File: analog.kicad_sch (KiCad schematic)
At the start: 51 parts, among them J10 Sensor harness, U13 ADS1115

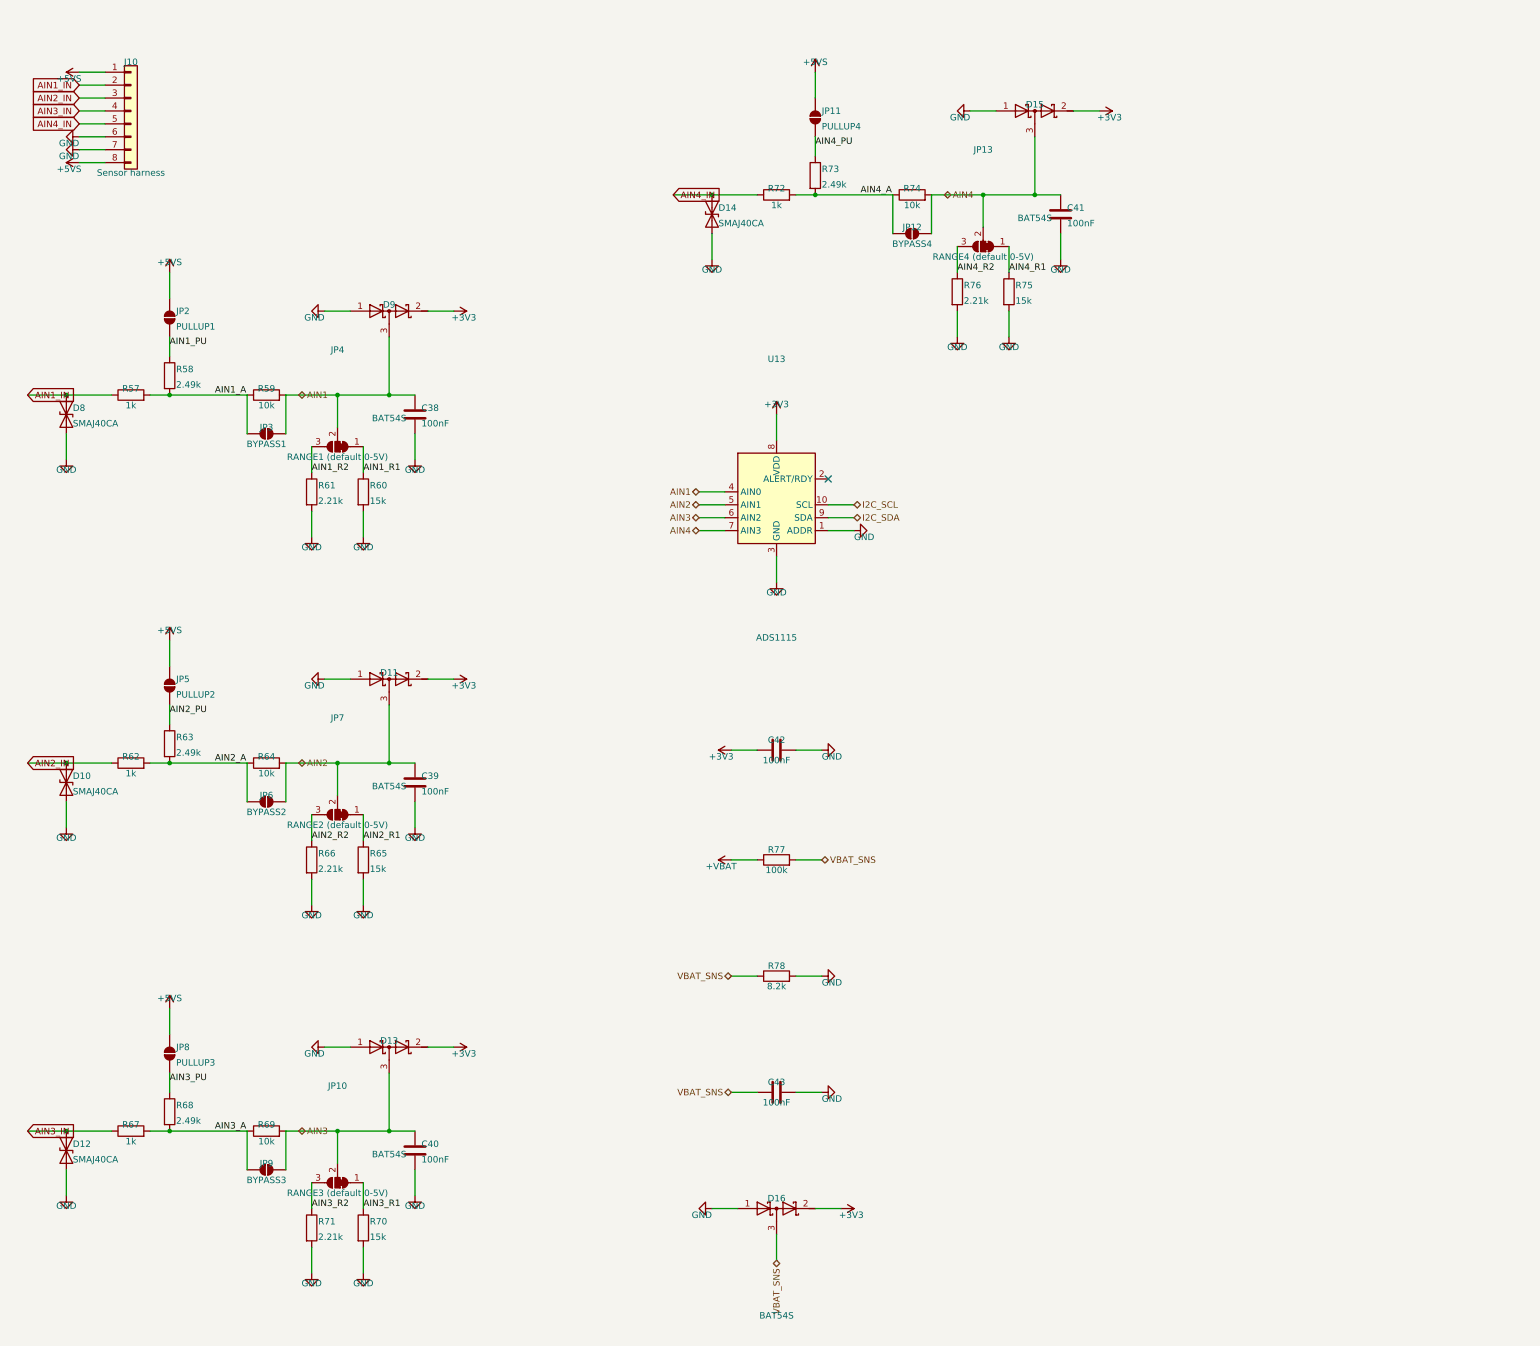
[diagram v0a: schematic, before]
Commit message: Re-scope the fork as a carrier board: no power section, differential analog, K-line
The shield idea does not survive measurement. Component courtyard on the
parent is 3052 mm2 over an 84 x 100 board -- 36% packing, not the 50% I had
been estimating -- and a DevKitC-1 is 63 x 25.5 = 1607 mm2. The parts alone
were 1.4x the whole dev board. So this is a carrier the dev board plugs into,
not a shield that fits on top of one.

Power section deleted entirely. It was 1746 mm2, 57% of the board, for two
rails the DevKitC-1 already makes from its USB-C. Gone: both LM5164 bucks and
everything around them, the LM74700 ideal diode, the reverse-battery FET, the
three electrolytic cans, the 12 V input, and the sensor-rail load switch.
Both rails are now inputs, taken up through the sockets -- which reverses the
earlier "feed 5 V only" rule, because there is no longer a second regulator
to parallel against.

Hold-up is a supercapacitor, not electrolytics. The first sizing was wrong:
energy goes as V-squared and the usable window at 5 V is 4.2 -> 3.6 V, so
2000 uF buys 12.5 ms, not the ~50 ms claimed. 0.5 F over the same window is
2.5 s, in less area than one of the 100 V cans it replaces. Low-ESR
cylindrical cells specifically -- coin EDLCs are 30-200 ohm and cannot source
120 mA at all.

Analog runs differentially. The board is grounded twice now, through the
sensor loom and through USB by way of a charger elsewhere in the car, and a
few hundred mV of chassis drop is 6% of a 0-5 V channel -- which makes the
0.1% dividers pointless. The correction has to be at the divider, not the
ADC, so the sensor ground comes back as a Kelvin wire through a matched
attenuator. Two ADS1115s, because one MUX only offers three channels against
a shared negative.

K-line added, discrete rather than an L9637D: that part's TXD threshold is
0.7*VCC = 3.5 V and a 3.3 V GPIO cannot meet it. Low-side 2N7002, clamped
22k/10k receiver, optional ISO 9141 tester pull-up on a jumper.

Pin map regrouped by boa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
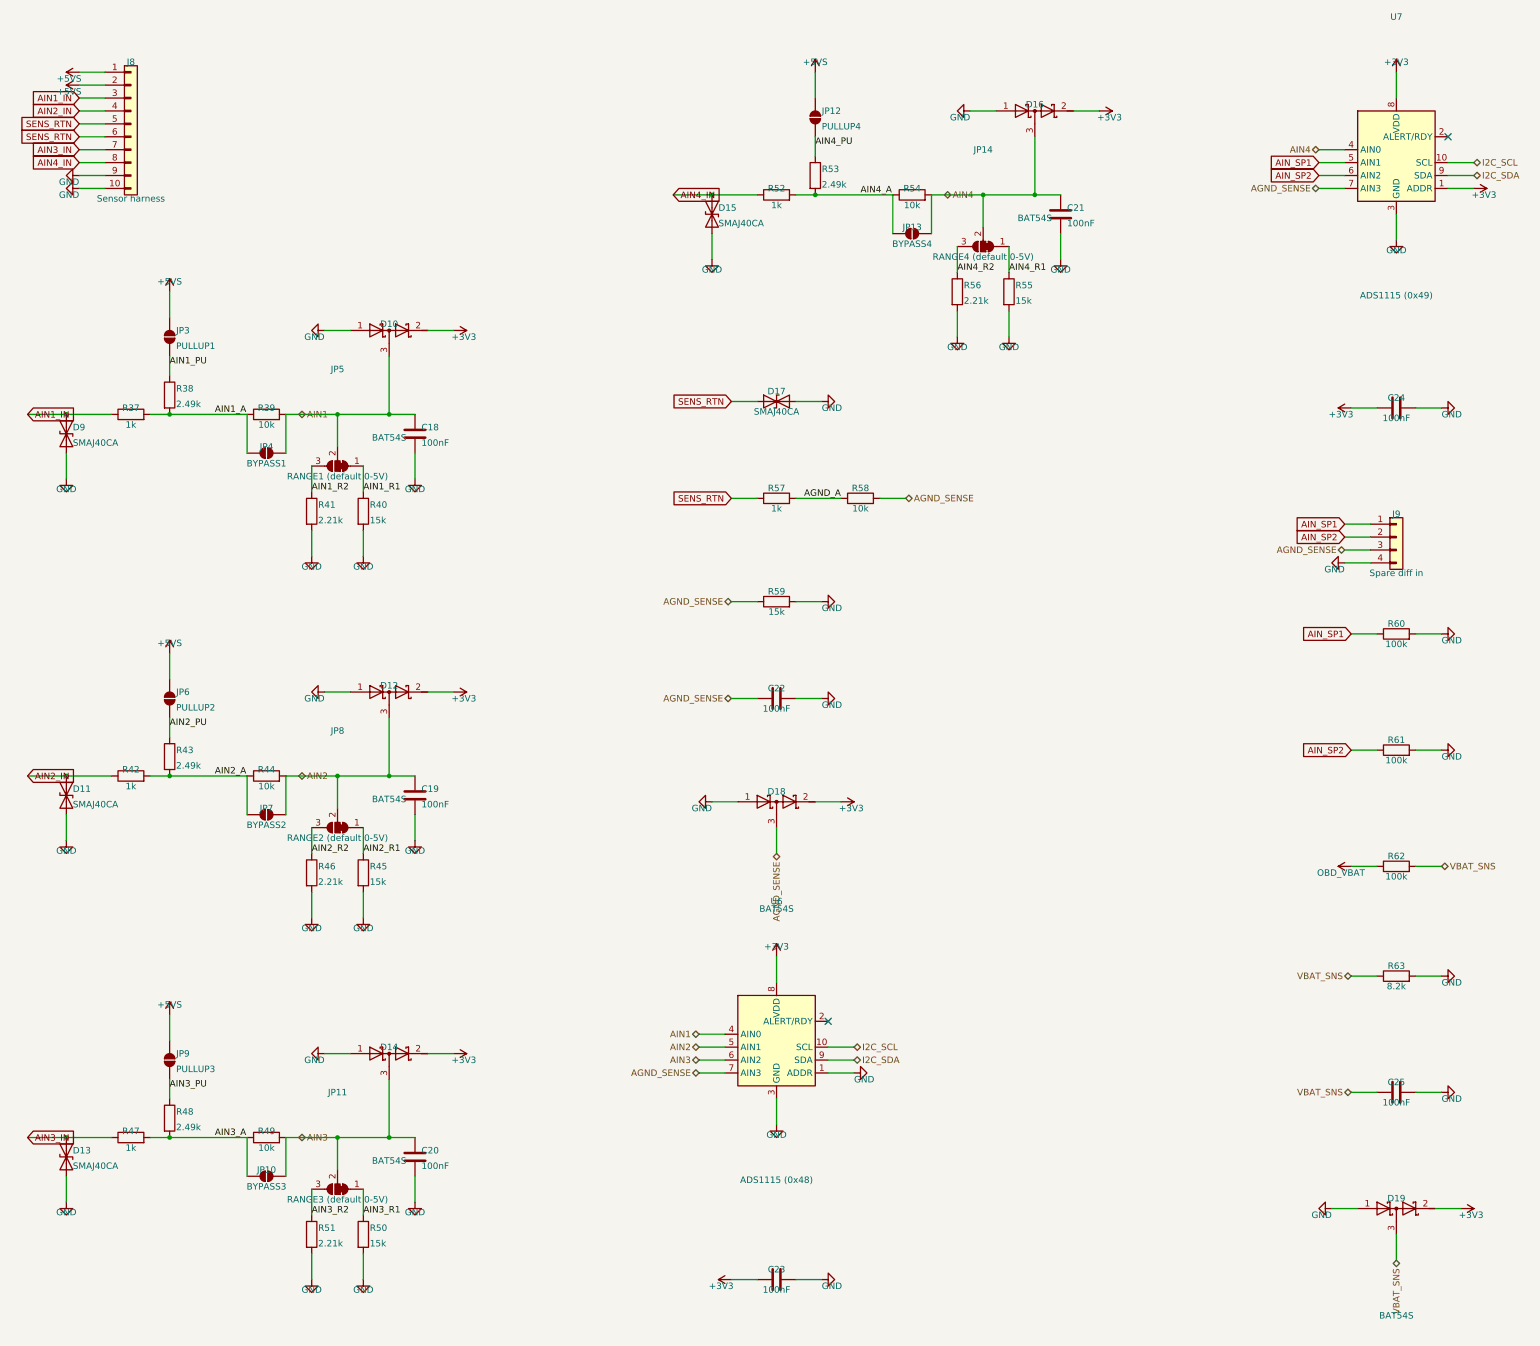
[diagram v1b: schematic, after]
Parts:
- removed C38, C39, C40, C41, C42, C43: 100nF, Capacitor_SMD:C_0805_2012Metric, symbol Device:C
- removed D8: SMAJ40CA, Diode_SMD:D_SMA, symbol Device:D_TVS
- removed J10: Sensor harness, Connector_JST:JST_PH_B8B-PH-K_1x08_P2.00mm_Vertical, symbol Connector_Generic:Conn_01x08
- removed JP2: PULLUP1, Jumper:SolderJumper-2_P1.3mm_Open_Pad1.0x1.5mm, symbol Jumper:SolderJumper_2_Open
- removed R64, R69, R74: 10k, Resistor_SMD:R_0805_2012Metric, symbol Device:R
- removed R65, R70, R75: 15k, Resistor_SMD:R_0805_2012Metric, symbol Device:R
- removed R66, R71, R76: 2.21k, Resistor_SMD:R_0805_2012Metric, symbol Device:R
- removed R67, R72: 1k, Resistor_SMD:R_0805_2012Metric, symbol Device:R
- removed R68, R73: 2.49k, Resistor_SMD:R_0805_2012Metric, symbol Device:R
- removed R77: 100k, Resistor_SMD:R_0805_2012Metric, symbol Device:R
- removed R78: 8.2k, Resistor_SMD:R_0805_2012Metric, symbol Device:R
- removed U13: ADS1115, Package_SO:VSSOP-10_3x3mm_P0.5mm, symbol Analog_ADC:ADS1115IDGS
- added C18, C19, C20, C21, C22, C23, C24, C25: 100nF, Capacitor_SMD:C_0805_2012Metric, symbol Device:C
- added D17: SMAJ40CA, Diode_SMD:D_SMA, symbol Device:D_TVS
- added D18, D19: BAT54S, Package_TO_SOT_SMD:SOT-23, symbol Device:D_Schottky_Dual_Series_AKC
- added J8: Sensor harness, Connector_JST:JST_PH_B10B-PH-K_1x10_P2.00mm_Vertical, symbol Connector_Generic:Conn_01x10
- added J9: Spare diff in, Connector_PinHeader_2.54mm:PinHeader_1x04_P2.54mm_Vertical, symbol Connector_Generic:Conn_01x04
- added JP14: RANGE4 (default 0-5V), Jumper:SolderJumper-3_P1.3mm_Bridged12_Pad1.0x1.5mm, symbol Jumper:SolderJumper_3_Bridged12
- added R37, R42, R47, R52: 1k, Resistor_SMD:R_0805_2012Metric, symbol Device:R
- added R38, R43, R48, R53: 2.49k, Resistor_SMD:R_0805_2012Metric, symbol Device:R
- added R39, R44, R49, R54: 10k, Resistor_SMD:R_0805_2012Metric, symbol Device:R
- added R40, R45, R50, R55: 15k, Resistor_SMD:R_0805_2012Metric, symbol Device:R
- added R41, R46, R51, R56: 2.21k, Resistor_SMD:R_0805_2012Metric, symbol Device:R
- added U6: ADS1115 (0x48), Package_SO:VSSOP-10_3x3mm_P0.5mm, symbol Analog_ADC:ADS1115IDGS
- added U7: ADS1115 (0x49), Package_SO:VSSOP-10_3x3mm_P0.5mm, symbol Analog_ADC:ADS1115IDGS
- D10: value SMAJ40CA -> BAT54S; footprint Diode_SMD:D_SMA -> Package_TO_SOT_SMD:SOT-23; symbol Device:D_TVS -> Device:D_Schottky_Dual_Series_AKC; MPN Littelfuse SMAJ40CA -> MDD BAT54S; Note Ch2 harness transient clamp (bidirectional, 400W) -> Ch1 rail clamp (both polarities)
- D11: value BAT54S -> SMAJ40CA; footprint Package_TO_SOT_SMD:SOT-23 -> Diode_SMD:D_SMA; symbol Device:D_Schottky_Dual_Series_AKC -> Device:D_TVS; MPN MDD BAT54S -> Littelfuse SMAJ40CA; Note Ch2 rail clamp (both polarities) -> Ch2 harness transient clamp (bidirectional, 400W)
- D12: value SMAJ40CA -> BAT54S; footprint Diode_SMD:D_SMA -> Package_TO_SOT_SMD:SOT-23; symbol Device:D_TVS -> Device:D_Schottky_Dual_Series_AKC; MPN Littelfuse SMAJ40CA -> MDD BAT54S; Note Ch3 harness transient clamp (bidirectional, 400W) -> Ch2 rail clamp (both polarities)
- D13: value BAT54S -> SMAJ40CA; footprint Package_TO_SOT_SMD:SOT-23 -> Diode_SMD:D_SMA; symbol Device:D_Schottky_Dual_Series_AKC -> Device:D_TVS; MPN MDD BAT54S -> Littelfuse SMAJ40CA; Note Ch3 rail clamp (both polarities) -> Ch3 harness transient clamp (bidirectional, 400W)
- D14: value SMAJ40CA -> BAT54S; footprint Diode_SMD:D_SMA -> Package_TO_SOT_SMD:SOT-23; symbol Device:D_TVS -> Device:D_Schottky_Dual_Series_AKC; MPN Littelfuse SMAJ40CA -> MDD BAT54S; Note Ch4 harness transient clamp (bidirectional, 400W) -> Ch3 rail clamp (both polarities)
- D15: value BAT54S -> SMAJ40CA; footprint Package_TO_SOT_SMD:SOT-23 -> Diode_SMD:D_SMA; symbol Device:D_Schottky_Dual_Series_AKC -> Device:D_TVS; MPN MDD BAT54S -> Littelfuse SMAJ40CA; Note Ch4 rail clamp (both polarities) -> Ch4 harness transient clamp (bidirectional, 400W)
- D16: Note Battery-monitor clamp -> Ch4 rail clamp (both polarities)
- D9: value BAT54S -> SMAJ40CA; footprint Package_TO_SOT_SMD:SOT-23 -> Diode_SMD:D_SMA; symbol Device:D_Schottky_Dual_Series_AKC -> Device:D_TVS; MPN MDD BAT54S -> Littelfuse SMAJ40CA; Note Ch1 rail clamp (both polarities) -> Ch1 harness transient clamp (bidirectional, 400W)
- JP10: value RANGE3 (default 0-5V) -> BYPASS3; footprint Jumper:SolderJumper-3_P1.3mm_Bridged12_Pad1.0x1.5mm -> Jumper:SolderJumper-2_P1.3mm_Open_Pad1.0x1.5mm; symbol Jumper:SolderJumper_3_Bridged12 -> Jumper:SolderJumper_2_Open; Note Ships BRIDGED 1-2 = the 0-5V range, which is what almost ev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 -> Close for a raw 0-3.3V sensor (shorts the upper leg)
- JP11: value PULLUP4 -> RANGE3 (default 0-5V); footprint Jumper:SolderJumper-2_P1.3mm_Open_Pad1.0x1.5mm -> Jumper:SolderJumper-3_P1.3mm_Bridged12_Pad1.0x1.5mm; symbol Jumper:SolderJumper_2_Open -> Jumper:SolderJumper_3_Bridged12; Note Close for 2-wire NTC / open-collector sensors -> Ships BRIDGED 1-2 = the 0-5V range, which is what almost ev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
- JP12: value BYPASS4 -> PULLUP4; Note Close for a raw 0-3.3V sensor (shorts the upper leg) -> Close for 2-wire NTC / open-collector sensors
- JP13: value RANGE4 (default 0-5V) -> BYPASS4; footprint Jumper:SolderJumper-3_P1.3mm_Bridged12_Pad1.0x1.5mm -> Jumper:SolderJumper-2_P1.3mm_Open_Pad1.0x1.5mm; symbol Jumper:SolderJumper_3_Bridged12 -> Jumper:SolderJumper_2_Open; Note Ships BRIDGED 1-2 = the 0-5V range, which is what almost ev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 -> Close for a raw 0-3.3V sensor (shorts the upper leg)
- JP3: value BYPASS1 -> PULLUP1; Note Close for a raw 0-3.3V sensor (shorts the upper leg) -> Close for 2-wire NTC / open-collector sensors
- JP4: value RANGE1 (default 0-5V) -> BYPASS1; footprint Jumper:SolderJumper-3_P1.3mm_Bridged12_Pad1.0x1.5mm -> Jumper:SolderJumper-2_P1.3mm_Open_Pad1.0x1.5mm; symbol Jumper:SolderJumper_3_Bridged12 -> Jumper:SolderJumper_2_Open; Note Ships BRIDGED 1-2 = the 0-5V range, which is what almost ev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 -> Close for a raw 0-3.3V sensor (shorts the upper leg)
- JP5: value PULLUP2 -> RANGE1 (default 0-5V); footprint Jumper:SolderJumper-2_P1.3mm_Open_Pad1.0x1.5mm -> Jumper:SolderJumper-3_P1.3mm_Bridged12_Pad1.0x1.5mm; symbol Jumper:SolderJumper_2_Open -> Jumper:SolderJumper_3_Bridged12; Note Close for 2-wire NTC / open-collector sensors -> Ships BRIDGED 1-2 = the 0-5V range, which is what almost ev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
- JP6: value BYPASS2 -> PULLUP2; Note Close for a raw 0-3.3V sensor (shorts the upper leg) -> Close for 2-wire NTC / open-collector sensors
- JP7: value RANGE2 (default 0-5V) -> BYPASS2; footprint Jumper:SolderJumper-3_P1.3mm_Bridged12_Pad1.0x1.5mm -> Jumper:SolderJumper-2_P1.3mm_Open_Pad1.0x1.5mm; symbol Jumper:SolderJumper_3_Bridged12 -> Jumper:SolderJumper_2_Open; Note Ships BRIDGED 1-2 = the 0-5V range, which is what almost ev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 -> Close for a raw 0-3.3V sensor (shorts the upper leg)
- JP8: value PULLUP3 -> RANGE2 (default 0-5V); footprint Jumper:SolderJumper-2_P1.3mm_Open_Pad1.0x1.5mm -> Jumper:SolderJumper-3_P1.3mm_Bridged12_Pad1.0x1.5mm; symbol Jumper:SolderJumper_2_Open -> Jumper:SolderJumper_3_Bridged12; Note Close for 2-wire NTC / open-collector sensors -> Ships BRIDGED 1-2 = the 0-5V range, which is what almost ev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
- JP9: value BYPASS3 -> PULLUP3; Note Close for a raw 0-3.3V sensor (shorts the upper leg) -> Close for 2-wire NTC / open-collector sensors
- R57: Note Ch1 series/fault-current limit; 0.1% thin film -- it is ins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 -> Matches the channels' 1k series
- R58: value 2.49k -> 10k; Note Ch1 bias resistor -> Matches the channels' upper leg; Tolerance (none) -> 0.1%
- R59: value 10k -> 15k; Note Ch1 divider upper leg, 0.1% thin film for AFR-grade accuracy -> Matches the channels' 0-5V lower leg. Also what holds AGND_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
- R60: value 15k -> 100k; Note 0-5V range: 5.0V in -> ~2.88V at the ADC (1k series include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 -> Bleed: an open input is not a reading; Tolerance 0.1% -> (none)
- R61: value 2.21k -> 100k; Note 0-16V range: 16.0V in -> ~2.67V at the ADC (1k series inclu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 -> (none); Tolerance 0.1% -> (none)
- R62: value 1k -> 100k; Note Ch2 series/fault-current limit; 0.1% thin film -- it is ins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 -> Battery monitor, upper leg; Tolerance 0.1% -> (none)
- R63: value 2.49k -> 8.2k; Note Ch2 bias resistor -> Divide by 13.2, not 11: at 36V the 11:1 divider put 3.27V o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
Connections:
- net +3V3: now also D10.2 (K), D12.2 (K), D14.2 (K), C23.1, C24.1, D18.2 (K), D19.2 (K), U6.8 (VDD), U7.1 (ADDR), U7.8 (VDD); no longer D11.2 (K), D13.2 (K), D15.2 (K), D9.2 (K)
- net +5VS: now also JP12.1 (A), JP3.1 (A), JP6.1 (A), JP9.1 (A), J8.1 (Pin_1), J8.2 (Pin_2); no longer JP11.1 (A), JP5.1 (A), JP8.1 (A)
- net AIN1: now also D10.3 (common), JP5.2 (C), C18.1, R39.2, U6.4 (AIN0); no longer D9.3 (common), JP3.2 (B), R59.2
- net AIN1_A: now also JP4.1 (A), R37.2, R38.2, R39.1; no longer JP3.1 (A), R57.2, R58.2, R59.1
- net AIN1_IN: now also D9.1 (A1), J8.3 (Pin_3), R37.1; no longer R57.1
- net AIN1_PU: now also JP3.2 (B), R38.1; no longer R58.1
- net AIN1_R1: now also JP5.1 (A), R40.1; no longer JP4.1 (A), R60.1
- net AIN1_R2: now also JP5.3 (B), R41.1; no longer JP4.3 (B), R61.1
- net AIN2: now also D12.3 (common), JP8.2 (C), C19.1, R44.2, U6.5 (AIN1); no longer D11.3 (common), JP6.2 (B)
- net AIN2_A: now also JP7.1 (A), R42.2, R43.2, R44.1; no longer JP6.1 (A), R62.2, R63.2
- net AIN2_IN: now also D11.1 (A1), J8.4 (Pin_4), R42.1; no longer D10.1 (A1), R62.1
- net AIN2_PU: now also JP6.2 (B), R43.1; no longer JP5.2 (B), R63.1
- net AIN2_R1: now also JP8.1 (A), R45.1; no longer JP7.1 (A)
- net AIN2_R2: now also JP8.3 (B), R46.1; no longer JP7.3 (B)
- net AIN3: now also D14.3 (common), JP11.2 (C), C20.1, R49.2, U6.6 (AIN2); no longer D13.3 (common), JP9.2 (B)
- net AIN3_A: now also JP10.1 (A), R47.2, R48.2, R49.1; no longer JP9.1 (A)
- net AIN3_IN: now also D13.1 (A1), J8.7 (Pin_7), R47.1; no longer D12.1 (A1)
- net AIN3_PU: now also JP9.2 (B), R48.1; no longer JP8.2 (B)
- net AIN3_R1: now also JP11.1 (A), R50.1; no longer JP10.1 (A)
- net AIN3_R2: now also JP11.3 (B), R51.1; no longer JP10.3 (B)
- net AIN4: now also D16.3 (common), C21.1, JP14.2 (C), R54.2, U7.4 (AIN0); no longer D15.3 (common), JP12.2 (B)
- net AIN4_A: now also JP13.1 (A), R52.2, R53.2, R54.1; no longer JP12.1 (A)
- net AIN4_IN: now also D15.1 (A1), J8.8 (Pin_8), R52.1; no longer D14.1 (A1)
- net AIN4_PU: now also JP12.2 (B), R53.1; no longer JP11.2 (B)
- net AIN4_R1: now also JP14.1 (A), R55.1; no longer JP13.1 (A)
- net AIN4_R2: now also JP14.3 (B), R56.1; no longer JP13.3 (B)
- net GND: now also D10.1 (A), D11.2 (A2), D12.1 (A), D13.2 (A2), D14.1 (A), D15.2 (A2), D9.2 (A2), R59.2, R63.2, C18.2, C19.2, C20.2, C21.2, C22.2, C23.2, C24.2, C25.2, D17.2 (A2), D18.1 (A), D19.1 (A), J8.10 (Pin_10), J8.9 (Pin_9), J9.4 (Pin_4), R40.2, R41.2, R45.2, R46.2, R50.2, R51.2, R55.2, R56.2, U6.1 (ADDR), U6.3 (GND), U7.3 (GND); no longer D10.2 (A2), D11.1 (A), D12.2 (A2), D13.1 (A), D14.2 (A2), D15.1 (A), D9.1 (A)
- net I2C_SCL: now also U6.10 (SCL), U7.10 (SCL)
- net I2C_SDA: now also U6.9 (SDA), U7.9 (SDA)
- net VBAT_SNS: now also R62.2, R63.1, C25.1, D19.3 (common); no longer D16.3 (common)
- new net AGND_A: R57.2, R58.1
- new net AGND_SENSE: C22.1, D18.3 (common), J9.3 (Pin_3), R58.2, R59.1, U6.7 (AIN3), U7.7 (AIN3)
- new net AIN_SP1: J9.1 (Pin_1), R60.1, U7.5 (AIN1)
- new net AIN_SP2: J9.2 (Pin_2), R61.1, U7.6 (AIN2)
- new net OBD_VBAT: R62.1
- new net SENS_RTN: D17.1 (A1), J8.5 (Pin_5), J8.6 (Pin_6), R57.1
- no-connect marks 1 -> 2
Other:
- moved on the sheet: D16, JP12, JP3, JP6, JP9, R57, R58, R59, R60, R61, R62, R63
